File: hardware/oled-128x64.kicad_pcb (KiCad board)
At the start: 2 copper layers, 40 x 40 mm, 24 parts, among them P1 CON-SENSOR, U1 M24C64, U2 OLED013, U3 DRILL, U4 DRILL, U5 DRILL, U6 DRILL

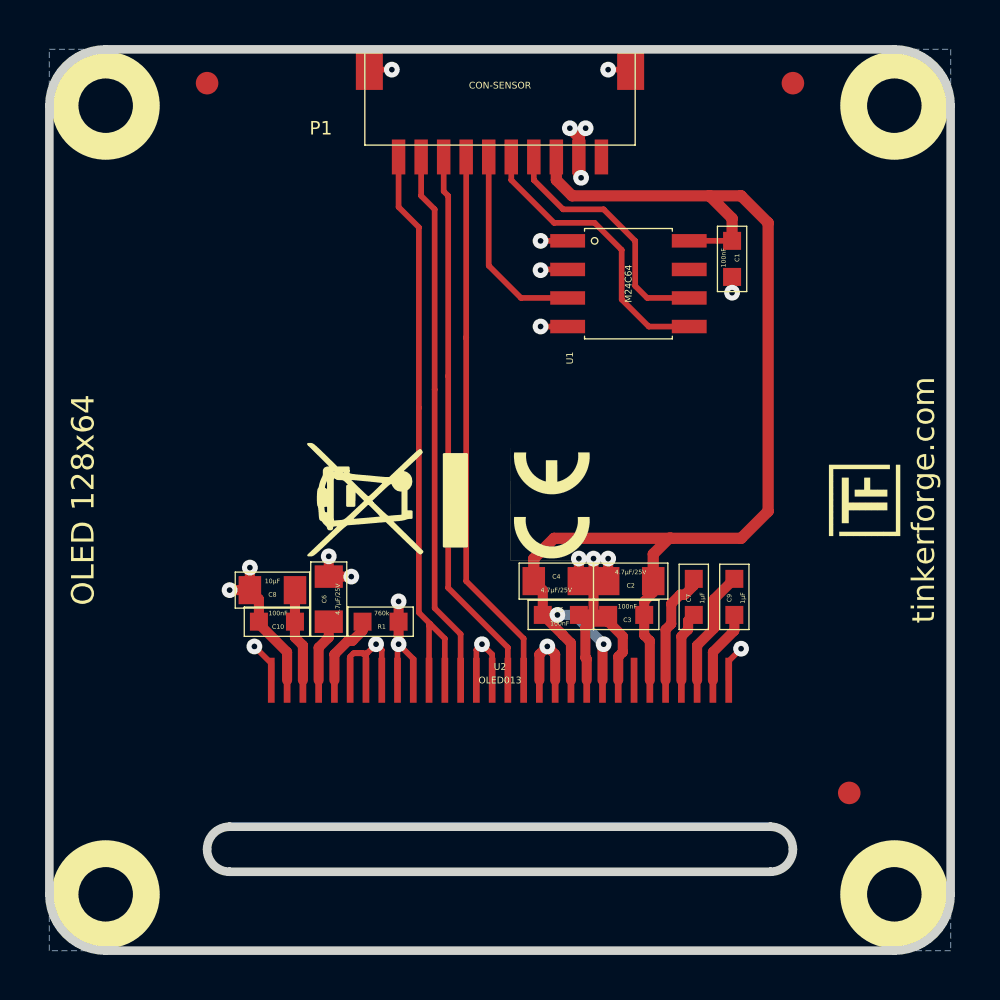
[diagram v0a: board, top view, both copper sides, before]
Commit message: put module description to the front
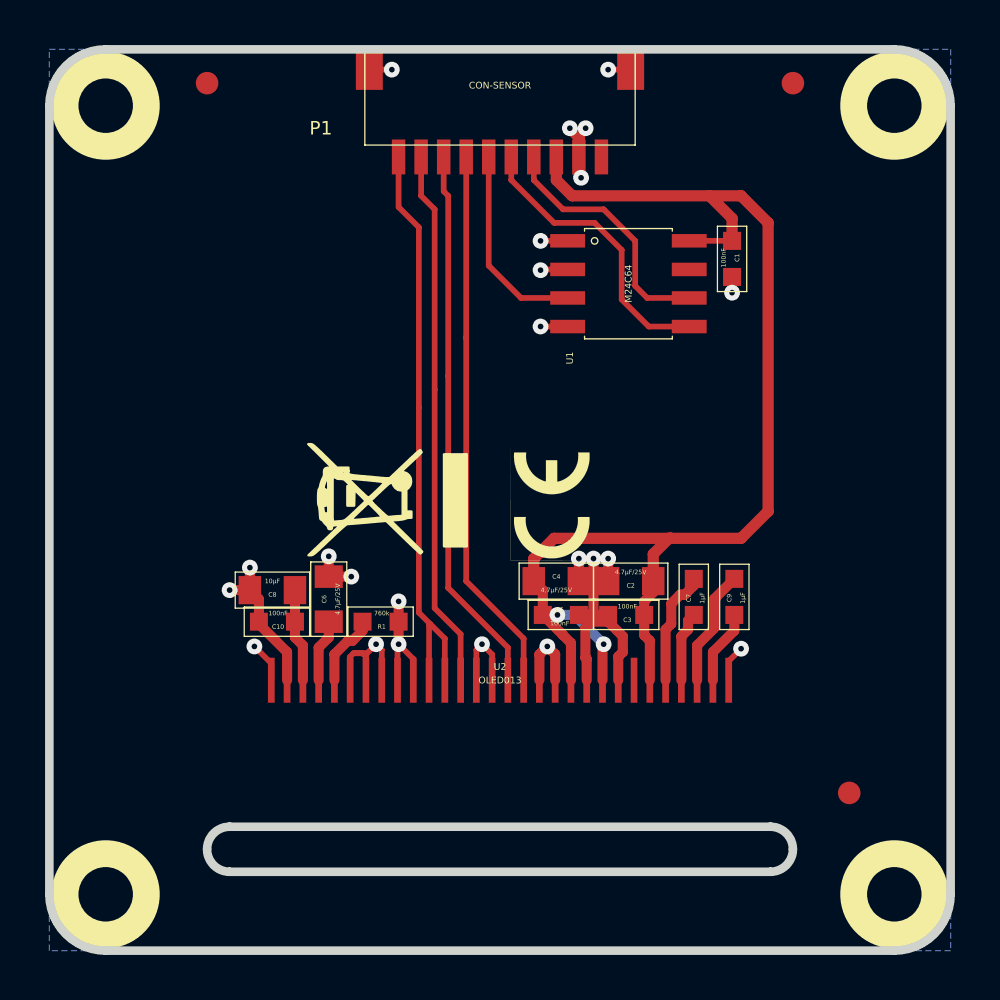
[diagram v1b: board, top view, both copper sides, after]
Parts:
- removed the G*** at (168.7, 143.2)
- added G***: LOGO, kicad-libraries:Logo_31x31m, B.Cu at (155.6, 124.7)

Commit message: add i2c pullup
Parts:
- added RP1: 2k2, kicad-libraries:0603X4, F.Cu at (155.5, 137.3)
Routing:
- net 3V3: track 57.5 -> 75.3 mm
- net Net-(P1-Pad10): track 26.6 -> 31.0 mm, vias 0 -> 2
- net Net-(P1-Pad9): track 24.0 -> 27.6 mm, vias 0 -> 2
- net Net-(P1-Pad8): track 24.4 -> 27.1 mm, vias 0 -> 2
- net Net-(P1-Pad7): track 24.3 -> 26.3 mm

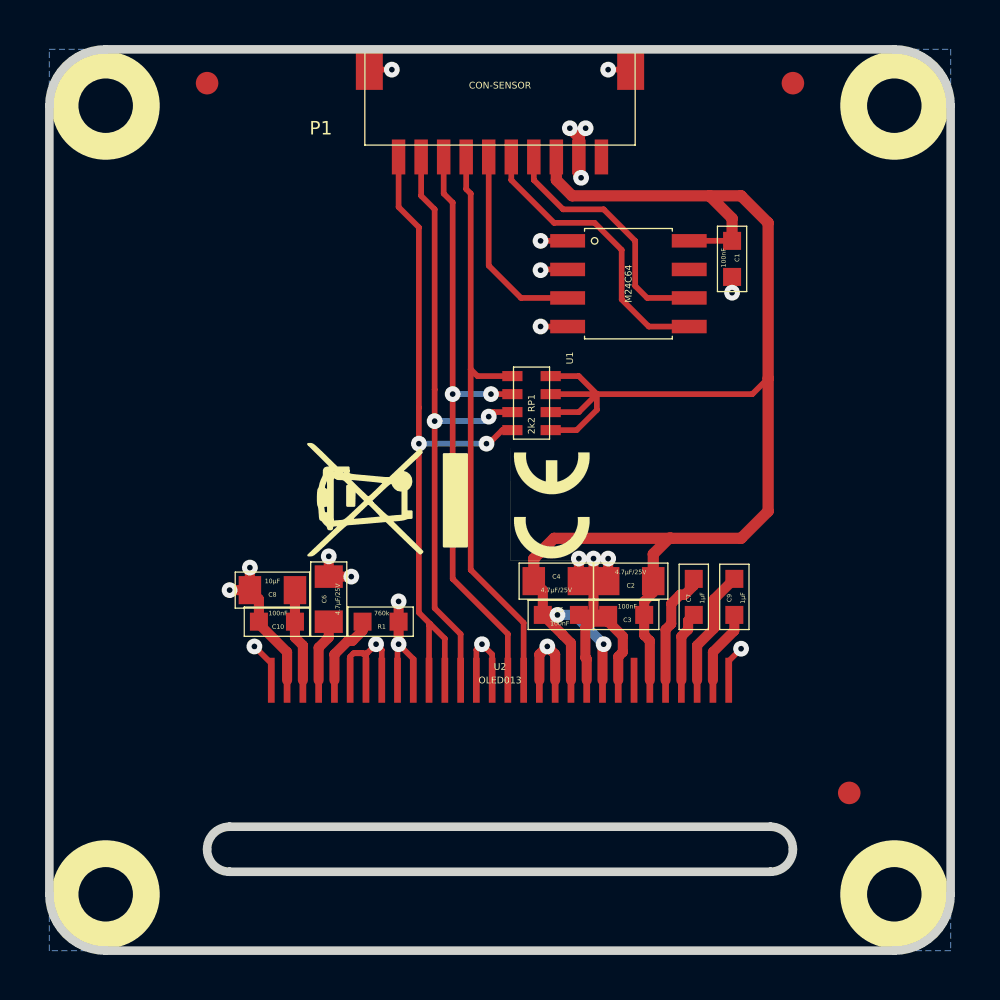
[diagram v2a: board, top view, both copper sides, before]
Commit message: add nand for reset line
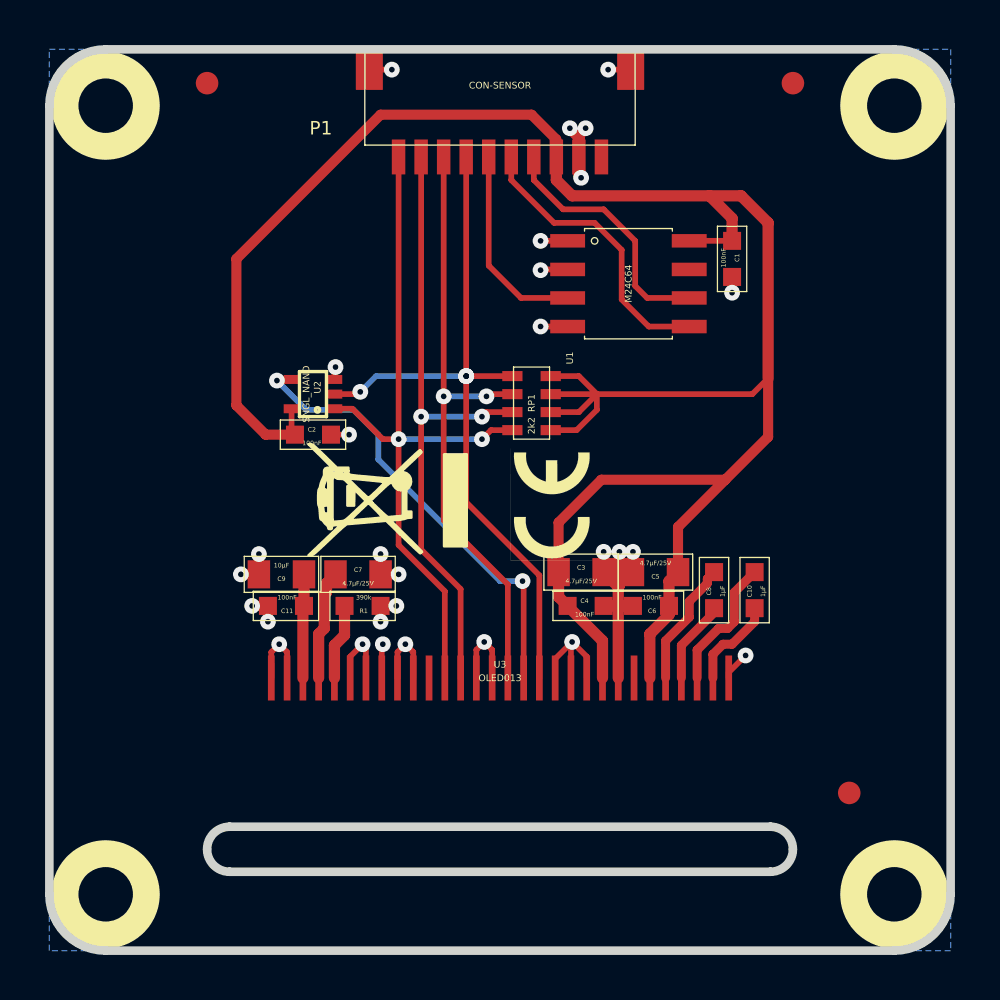
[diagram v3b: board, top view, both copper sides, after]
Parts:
- added C11: 100nF, kicad-libraries:0603, F.Cu at (144.6, 146.3)
- added U7: DRILL, kicad-libraries:DRILL_NP, F.Cu at (136.6, 159.1)
- C10: value 100nF -> 1µF
- C2, C4, C6: value 4.7µF/25V -> 100nF; footprint kicad-libraries:0805 -> kicad-libraries:0603
- C3, C5: value 100nF -> 4.7µF/25V; footprint kicad-libraries:0603 -> kicad-libraries:0805
- C7: value 1µF -> 4.7µF/25V; footprint kicad-libraries:0603 -> kicad-libraries:0805
- C8: value 10µF -> 1µF; footprint kicad-libraries:0805 -> kicad-libraries:0603
- C9: value 1µF -> 10µF; footprint kicad-libraries:0603 -> kicad-libraries:0805
- R1: value 760k -> 390k
- U2: value OLED013 -> SNGL_NAND; footprint kicad-libraries:OLED013 -> kicad-libraries:SC70-5
- U3: value DRILL -> OLED013; footprint kicad-libraries:DRILL_NP -> kicad-libraries:OLED013
- moved C10 21.2 mm to (165.4, 145.6), turned to 270 degrees
- moved C9 20.1 mm to (144.4, 144.9), turned to 0 degrees
- moved U3 20.0 mm to (154.1, 149.5), turned to 180 degrees
- moved C8 19.6 mm to (163.6, 145.6), turned to 270 degrees
- moved C2 15.5 mm to (145.8, 138.7), turned to 180 degrees
- moved U2 15.2 mm to (145.8, 136.9), turned to 90 degrees
- moved C7 14.9 mm to (147.8, 144.9), turned to 180 degrees
- moved C6 14.3 mm to (160.8, 146.3), turned to 0 degrees
- moved C5 4.61 mm to (161.0, 144.8), turned to 0 degrees
- moved C3 2.76 mm to (157.7, 144.8), turned to 180 degrees
- moved C4 1.70 mm to (157.9, 146.3)
- moved R1 1.06 mm to (148.0, 146.3)
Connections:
- C10 pad 1: GND -> Net-(C10-Pad1)
- C6 pad 2: Net-(C6-Pad2) -> 3V3
- C7 pad 1: Net-(C7-Pad1) -> GND
- C8 pad 1: GND -> Net-(C8-Pad1)
- C8 pad 2: Net-(C10-Pad2) -> Net-(C8-Pad2)
- C9 pad 1: Net-(C9-Pad1) -> GND
- C9 pad 2: Net-(C9-Pad2) -> Net-(C11-Pad2)
- U2 pad 1: GND -> Net-(P1-Pad10)
- U2 pad 2: Net-(C9-Pad2) -> Net-(P1-Pad7)
- U2 pad 3: Net-(C9-Pad1) -> GND
- U2 pad 4: Net-(C7-Pad2) -> Net-(U2-Pad4)
- U2 pad 5: Net-(C7-Pad1) -> 3V3
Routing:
- net 3V3: track 75.3 -> 100.5 mm, vias 2 -> 0
- net Net-(U2-Pad4): track 0.00 -> 20.2 mm, vias 0 -> 2
- net Net-(P1-Pad7): track 26.3 -> 32.7 mm, vias 0 -> 3
- net Net-(C10-Pad1): track 0.00 -> 5.99 mm
- net Net-(C8-Pad1): track 0.00 -> 5.59 mm
- net Net-(C9-Pad1): track 5.18 -> 0.00 mm
- net Net-(C7-Pad1): track 5.14 -> 0.00 mm
- net Net-(C11-Pad2): track 0.00 -> 4.62 mm
- net Net-(C8-Pad2): track 0.00 -> 3.70 mm
- net Net-(C9-Pad2): track 3.29 -> 0.00 mm
- net GND: track 56.0 -> 53.0 mm, vias 23 -> 29
- net Net-(C6-Pad2): track 2.79 -> 0.00 mm
- net Net-(C7-Pad2): track 3.13 -> 4.91 mm
- net Net-(P1-Pad10): track 31.0 -> 32.6 mm

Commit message: change pullup to series resistor, fix routing
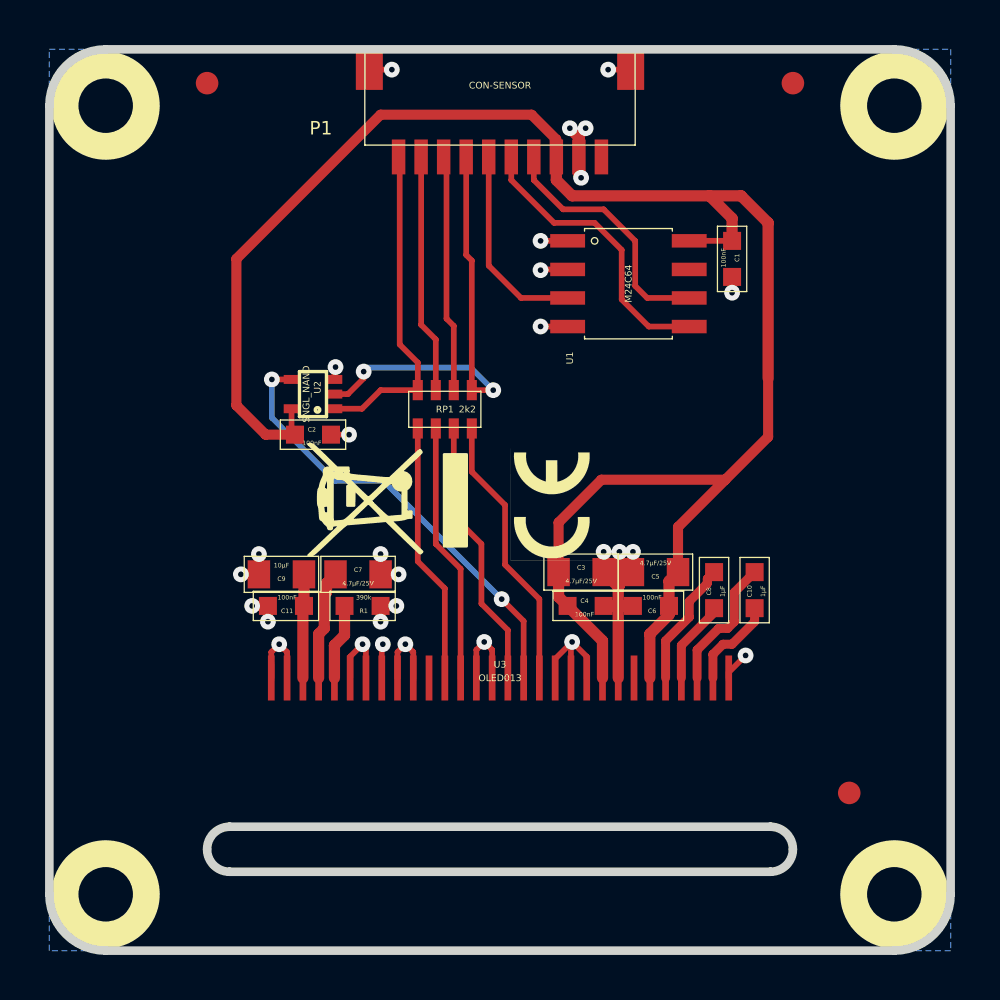
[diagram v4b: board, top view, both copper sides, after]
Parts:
- moved RP1 3.86 mm to (151.7, 137.6), turned to 0 degrees
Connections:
- RP1 pad 1: 3V3 -> Net-(P1-Pad7)
- RP1 pad 2: 3V3 -> Net-(P1-Pad8)
- RP1 pad 3: 3V3 -> Net-(P1-Pad9)
- RP1 pad 4: 3V3 -> Net-(P1-Pad10)
- RP1 pad 5: Net-(P1-Pad7) -> Net-(RP1-Pad5)
- RP1 pad 6: Net-(P1-Pad8) -> Net-(RP1-Pad6)
- RP1 pad 7: Net-(P1-Pad9) -> Net-(RP1-Pad7)
- RP1 pad 8: Net-(P1-Pad10) -> Net-(RP1-Pad8)
- U3 pad 13: Net-(P1-Pad7) -> Net-(RP1-Pad8)
- U3 pad 15: Net-(P1-Pad8) -> Net-(RP1-Pad7)
- U3 pad 18: Net-(P1-Pad9) -> Net-(RP1-Pad6)
- U3 pad 19: Net-(P1-Pad10) -> Net-(RP1-Pad5)
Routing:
- net Net-(P1-Pad10): track 32.6 -> 14.7 mm, vias 2 -> 0
- net 3V3: track 100.5 -> 82.7 mm
- net Net-(P1-Pad9): track 28.0 -> 10.6 mm, vias 2 -> 0
- net Net-(P1-Pad8): track 27.4 -> 10.5 mm, vias 2 -> 0
- net Net-(P1-Pad7): track 32.7 -> 19.5 mm, vias 3 -> 2
- net Net-(RP1-Pad8): track 0.00 -> 12.3 mm
- net Net-(RP1-Pad7): track 0.00 -> 12.1 mm
- net Net-(RP1-Pad5): track 0.00 -> 11.6 mm
- net Net-(RP1-Pad6): track 0.00 -> 11.5 mm

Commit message: add hardware version number
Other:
- board text added: "OLED 128x64 1.0"
- board text removed: "OLED 128x64"
